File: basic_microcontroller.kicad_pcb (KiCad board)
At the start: 4 copper layers, 70 x 70 mm, 81 parts, among them J1 USB_C_Receptacle_USB2.0, J2 AVR-ISP-6, J3 Screw_Terminal_01x02, U1 ATmega32U4-A, Y1 8MHz

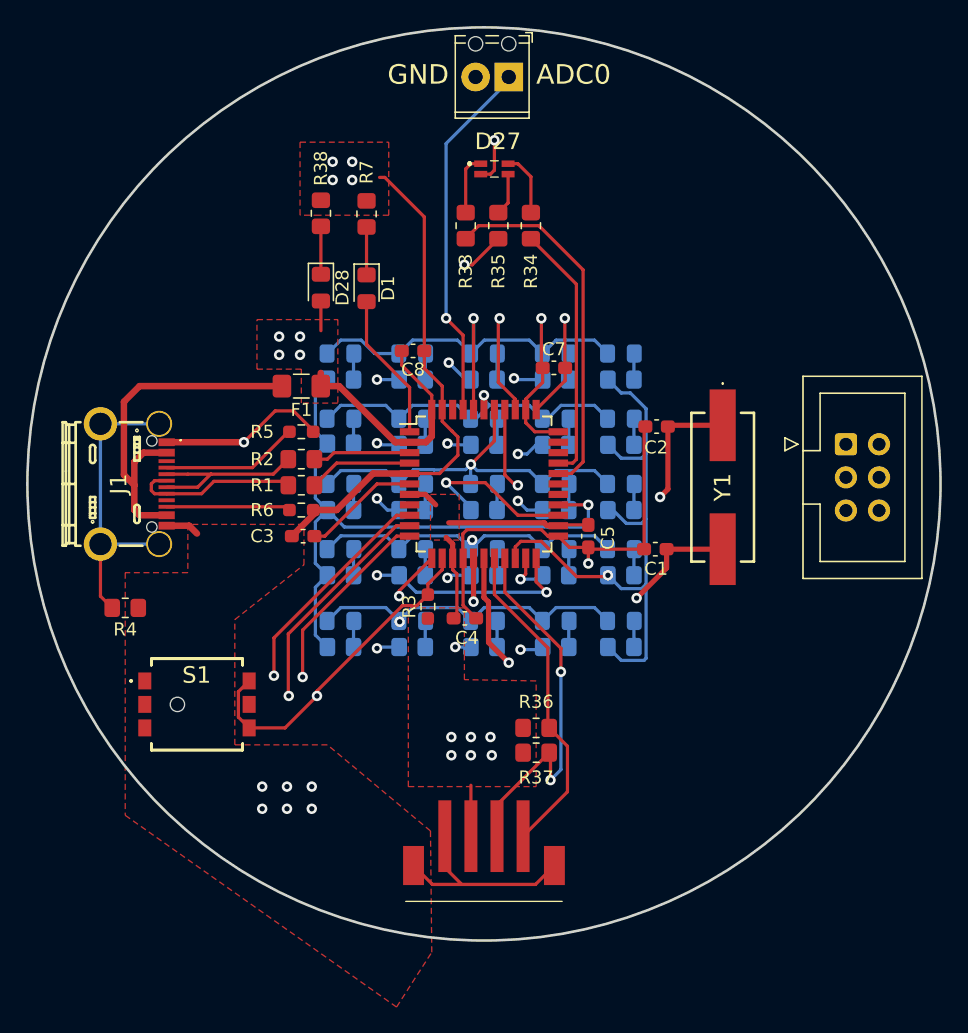
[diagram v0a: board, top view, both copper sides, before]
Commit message: Fixed wiring on button
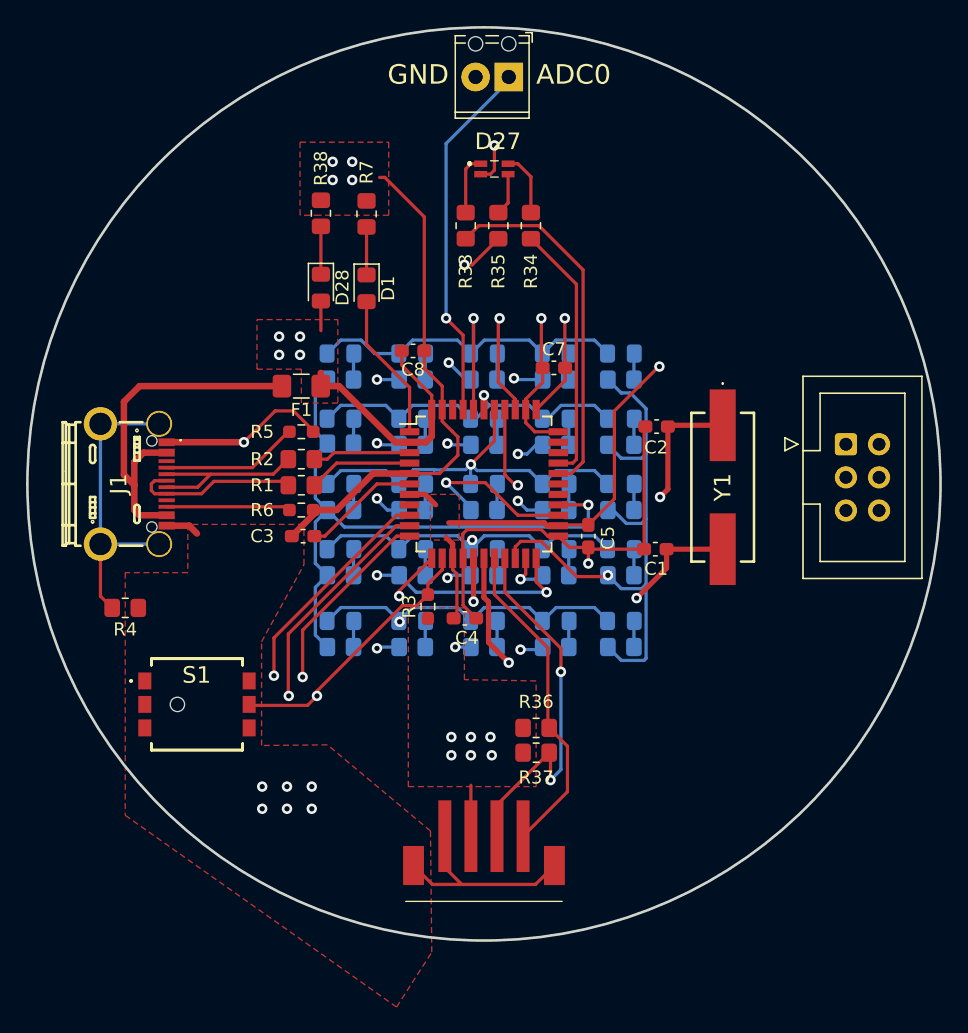
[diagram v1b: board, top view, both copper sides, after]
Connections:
- S1 pad 1: GND -> unconnected-(S1-COM_1-Pad1)
- S1 pad 3: GND -> unconnected-(S1-NC_1-Pad3)
- S1 pad 4: /RESET -> GND
- S1 pad 5: unconnected-(S1-NO_2-Pad5) -> /RESET
- S1 pad 6: /RESET -> unconnected-(S1-NC_2-Pad6)
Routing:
- net +5V: track 56.4 -> 70.4 mm, vias 12 -> 13
- net /RESET: track 72.7 -> 67.8 mm
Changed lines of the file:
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@@
   (net 66 "Net-(J3-Pin_1)")
   (net 67 "unconnected-(S1-NO_1-Pad2)")
-  (net 68 "unconnected-(S1-NO_2-Pad5)")
+  (net 68 "unconnected-(S1-COM_1-Pad1)")
   (net 69 "/SDA")
   (net 70 "unconnected-(J1-SBU1-PadA8)")
@@
   (net 73 "Net-(D27-K_GREEN)")
   (net 74 "Net-(D27-K_BLUE)")
+  (net 75 "unconnected-(S1-NC_1-Pad3)")
+  (net 76 "unconnected-(S1-NC_2-Pad6)")
   (footprint "Resistor_SMD:R_0603_1608Metric_Pad0.98x0.95mm_HandSolder" (layer "F.Cu")
     (at 136 96)
@@
     (pad "" np_thru_hole circle (at -1.5 0) (size 1.1 1.1) (drill 1.1) (layers "*.Cu" "*.Mask"))
     (pad "1" smd rect (at -4 -1.8) (size 1 1.3) (layers "F.Cu" "F.Paste" "F.Mask")
-      (net 1 "GND") (pinfunction "COM_1") (pintype "passive"))
+      (net 68 "unconnected-(S1-COM_1-Pad1)") (pinfunction "COM_1") (pintype "passive+no_connect"))
     (pad "2" smd rect (at -4 0) (size 1 1.3) (layers "F.Cu" "F.Paste" "F.Mask")
       (net 67 "unconnected-(S1-NO_1-Pad2)") (pinfunction "NO_1") (pintype "passive+no_connect"))
     (pad "3" smd rect (at -4 1.8) (size 1 1.3) (layers "F.Cu" "F.Paste" "F.Mask")
-      (net 1 "GND") (pinfunction "NC_1") (pintype "passive"))
+      (net 75 "unconnected-(S1-NC_1-Pad3)") (pinfunction "NC_1") (pintype "passive+no_connect"))
     (pad "4" smd rect (at 4 -1.8) (size 1 1.3) (layers "F.Cu" "F.Paste" "F.Mask")
-      (net 9 "/RESET") (pinfunction "COM_2") (pintype "passive"))
+      (net 1 "GND") (pinfunction "COM_2") (pintype "passive"))
     (pad "5" smd rect (at 4 0) (size 1 1.3) (layers "F.Cu" "F.Paste" "F.Mask")
-      (net 68 "unconnected-(S1-NO_2-Pad5)") (pinfunction "NO_2") (pintype "passive+no_connect"))
+      (net 9 "/RESET") (pinfunction "NO_2") (pintype "passive"))
     (pad "6" smd rect (at 4 1.8) (size 1 1.3) (layers "F.Cu" "F.Paste" "F.Mask")
-      (net 9 "/RESET") (pinfunction "NC_2") (pintype "passive"))
+      (net 76 "unconnected-(S1-NC_2-Pad6)") (pinfunction "NC_2") (pintype "passive+no_connect"))
     (model "${KIPRJMOD}/ThirdParty/SPEJ110100.stp"
       (offset (xyz 0 0 0))
@@
   (segment (start 141.8 100) (end 144.3 100) (width 0.25) (layer "F.Cu") (net 4))
   (segment (start 156.2 91.075) (end 156.2 87.3) (width 0.25) (layer "F.Cu") (net 5))
+  (segment (start 158 103.1375) (end 160 101.1375) (width 0.25) (layer "F.Cu") (net 5))
+  (segment (start 150.8 75.95) (end 150.8 74.05) (width 0.25) (layer "F.Cu") (net 5))
   (segment (start 145.55 96.8) (end 146 96.35) (width 0.5) (layer "F.Cu") (net 5))
   (segment (start 138.9 92.5) (end 137.4875 92.5) (width 0.5) (layer "F.Cu") (net 5))
   (segment (start 147.6625 110.3125) (end 147.675 110.3) (width 0.4) (layer "F.Cu") (net 5))
   (segment (start 147.6 104.6) (end 147.6 105.7) (width 0.4) (layer "F.Cu") (net 5))
-  (segment (start 150.8 75.95) (end 150.8 73.65) (width 0.25) (layer "F.Cu") (net 5))
   (segment (start 145.5 100.8) (end 146.3 101.6) (width 0.4) (layer "F.Cu") (net 5))
   (segment (start 156.225 92.075) (end 156.225 91.1) (width 0.25) (layer "F.Cu") (net 5))
-  (segment (start 150.5 76.25) (end 150.8 75.95) (width 0.25) (layer "F.Cu") (net 5))
   (segment (start 147.6 105.7) (end 147.6 106.574695) (width 0.25) (layer "F.Cu") (net 5))
+  (segment (start 160 94.4) (end 163.4 91) (width 0.25) (layer "F.Cu") (net 5))
   (segment (start 147.925 106.899695) (end 147.925 110.05) (width 0.25) (layer "F.Cu") (net 5))
   (segment (start 147.1 104.1) (end 147.6 104.6) (width 0.4) (layer "F.Cu") (net 5))
   (segment (start 144.3 96.8) (end 143.2 96.8) (width 0.5) (layer "F.Cu") (net 5))
   (segment (start 154 94.3) (end 156.225 92.075) (width 0.25) (layer "F.Cu") (net 5))
+  (segment (start 150.5 76.25) (end 150.8 75.95) (width 0.25) (layer "F.Cu") (net 5))
   (segment (start 154.842462 103.2) (end 154.617462 102.975) (width 0.4) (layer "F.Cu") (net 5))
   (segment (start 155.7625 103.1375) (end 155.7 103.2) (width 0.25) (layer "F.Cu") (net 5))
@@
   (segment (start 143.7 90.9) (end 143.7 89.8) (width 0.25) (layer "F.Cu") (net 5))
   (segment (start 144.3 100.8) (end 145.5 100.8) (width 0.4) (layer "F.Cu") (net 5))
+  (segment (start 163.4 91) (end 163.45 91) (width 0.25) (layer "F.Cu") (net 5))
   (segment (start 147.6 106.574695) (end 147.925 106.899695) (width 0.25) (layer "F.Cu") (net 5))
   (segment (start 149 127) (end 149 123.1) (width 0.25) (layer "F.Cu") (net 5))
@@
   (segment (start 143.2 96.8) (end 138.9 92.5) (width 0.5) (layer "F.Cu") (net 5))
   (segment (start 137.4875 91.4875) (end 137.4875 92.5) (width 0.5) (layer "F.Cu") (net 5))
-  (segment (start 149.75 76.25) (end 150.5 76.25) (width 0.25) (layer "F.Cu") (net 5))
   (segment (start 155.7 103.2) (end 154.842462 103.2) (width 0.4) (layer "F.Cu") (net 5))
   (segment (start 137.5 85.975) (end 137.5 88.25) (width 0.25) (layer "F.Cu") (net 5))
+  (segment (start 149.75 76.25) (end 150.5 76.25) (width 0.25) (layer "F.Cu") (net 5))
   (segment (start 154.617462 102.975) (end 147.3 102.975) (width 0.4) (layer "F.Cu") (net 5))
+  (segment (start 160 101.1375) (end 160 94.4) (width 0.25) (layer "F.Cu") (net 5))
   (segment (start 158 103.1375) (end 155.7625 103.1375) (width 0.25) (layer "F.Cu") (net 5))
   (segment (start 144.3 96.8) (end 145.55 96.8) (width 0.5) (layer "F.Cu") (net 5))
@@
   (via (at 150.5 119.4) (size 0.8) (drill 0.4) (layers "F.Cu" "B.Cu") (free) (net 5))
   (via (at 135.9 90.1) (size 0.8) (drill 0.4) (layers "F.Cu" "B.Cu") (net 5))
-  (via (at 150.8 73.65) (size 0.8) (drill 0.4) (layers "F.Cu" "B.Cu") (net 5))
+  (via (at 150.8 74.05) (size 0.8) (drill 0.4) (layers "F.Cu" "B.Cu") (net 5))
   (via (at 147.5 119.4) (size 0.8) (drill 0.4) (layers "F.Cu" "B.Cu") (free) (net 5))
   (via (at 149 120.8) (size 0.8) (drill 0.4) (layers "F.Cu" "B.Cu") (free) (net 5))
+  (via (at 163.45 91) (size 0.8) (drill 0.4) (layers "F.Cu" "B.Cu") (net 5))
   (segment (start 144.3 104) (end 143.3 104) (width 0.25) (layer "F.Cu") (net 6))
   (segment (start 143.3 104) (end 136.1 111.2) (width 0.25) (layer "F.Cu") (net 6))
@@
   (segment (start 136.68809 117.9) (end 160.4 117.9) (width 0.25) (layer "In2.Cu") (net 8))
   (segment (start 179.1 100.6825) (end 180.2875 99.495) (width 0.25) (layer "In2.Cu") (net 8))
+  (segment (start 132.0745 116.9745) (end 132 116.9) (width 0.25) (layer "F.Cu") (net 9))
   (segment (start 137.2 116.2495) (end 137.2 115.874695) (width 0.25) (layer "F.Cu") (net 9))
-  (segment (start 131.175 115.925) (end 132 115.1) (width 0.25) (layer "F.Cu") (net 9))
+  (segment (start 136.475 116.9745) (end 132.0745 116.9745) (width 0.25) (layer "F.Cu") (net 9))
   (segment (start 137.2 115.874695) (end 143.749695 109.325) (width 0.25) (layer "F.Cu") (net 9))
-  (segment (start 132 118.7) (end 131.175 117.875) (width 0.25) (layer "F.Cu") (net 9))
   (segment (start 146.8 106.575) (end 146.8 105.7) (width 0.25) (layer "F.Cu") (net 9))
   (segment (start 145.7 107.675) (end 146.8 106.575) (width 0.25) (layer "F.Cu") (net 9))
   (segment (start 143.749695 109.325) (end 144.8625 109.325) (width 0.25) (layer "F.Cu") (net 9))
-  (segment (start 134.7495 118.7) (end 132 118.7) (width 0.25) (layer "F.Cu") (net 9))
   (segment (start 145.7 108.4875) (end 145.7 107.675) (width 0.25) (layer "F.Cu") (net 9))
-  (segment (start 131.175 117.875) (end 131.175 115.925) (width 0.25) (layer "F.Cu") (net 9))
-  (segment (start 137.2 116.2495) (end 134.7495 118.7) (width 0.25) (layer "F.Cu") (net 9))
+  (segment (start 137.2 116.2495) (end 136.475 116.9745) (width 0.25) (layer "F.Cu") (net 9))
   (segment (start 144.8625 109.325) (end 145.7 108.4875) (width 0.25) (layer "F.Cu") (net 9))
   (via (at 137.2 116.2495) (size 0.8) (drill 0.4) (layers "F.Cu" "B.Cu") (net 9))
@@
   (segment (start 137 100.1) (end 138.7 98.4) (width 0.25) (layer "F.Cu") (net 11))
   (segment (start 125.675 100.25) (end 128.05 100.25) (width 0.25) (layer "F.Cu") (net 12))
-  (segment (start 129.05 99.25) (end 129.1 99.25) (width 0.25) (layer "F.Cu") (net 12))
-  (segment (start 127.3 99.25) (end 133.85 99.25) (width 0.25) (layer "F.Cu") (net 12))
-  (segment (start 125.675 99.25) (end 127.3 99.25) (width 0.25) (layer "F.Cu") (net 12))
-  (segment (start 128.05 100.25) (end 129.05 99.25) (width 0.25) (layer "F.Cu") (net 12))
+  (segment (start 125.675 99.25) (end 133.85 99.25) (width 0.25) (layer "F.Cu") (net 12))
   (segment (start 133.85 99.25) (end 135 98.1) (width 0.25) (layer "F.Cu") (net 12))
+  (segment (start 128.05 100.25) (end 129.05 99.25) (width 0.25) (layer "F.Cu") (net 12))
   (segment (start 138 98.1) (end 138.5 97.6) (width 0.25) (layer "F.Cu") (net 13))
   (segment (start 137 98.1) (end 138 98.1) (width 0.25) (layer "F.Cu") (net 13))
@@
         (xy 145.9 126.6)
         (xy 138 120)
-        (xy 130.9 120)
-        (xy 130.9 110.4)
+        (xy 132.95 120.05)
+        (xy 132.95 112.1)
         (xy 136.2 106.2)
         (xy 136.2 103.1)
@@
     (polygon
       (pts
-        (xy 111.7 59.9)
+        (xy 110.5 61.15)
         (xy 190.7 61.5)
         (xy 190.6 140.7)
